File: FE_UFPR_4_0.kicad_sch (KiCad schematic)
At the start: 0 parts

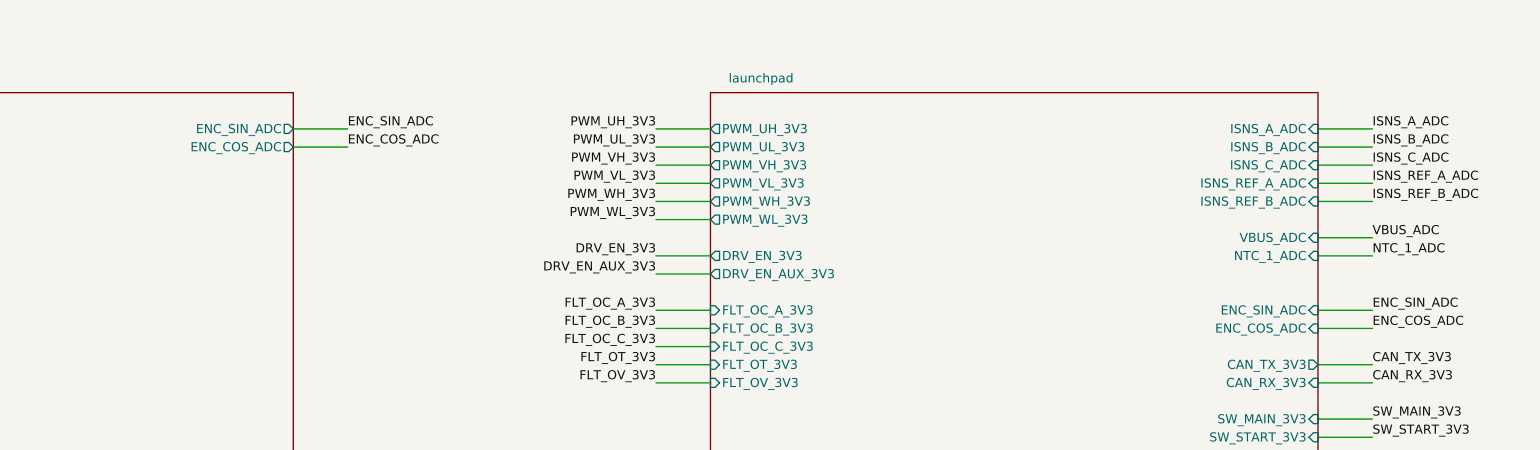
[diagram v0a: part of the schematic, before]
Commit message: S9.5: motor temperature channel (EMRAX KTY81-210) on J4 cavities 6/7
The board had no motor-temperature channel at all, and the EMRAX manual
makes one mandatory: the sensor "must be connected to the controller",
120 C on the copper windings voids the warranty, and on sensor
disconnection "the controller has to stop the motor". Captured now
because the board is placed but not yet routed.

Circuit: KTY81-210 as the divider's BOTTOM leg, excited from +3V3 through
R129 2.20k 0.1%. Open -> 3.30 V, short -> 0 V, both outside the valid
1.12-2.18 V band, so disconnect detection is free. +3V3 rather than +5V
so an open sensor cannot exceed the ADC's VDDA+0.3 absolute maximum.
6.25 codes/K at the 120 C limit. R131/R132 monitor the excitation rail on
ADCINA3 so firmware cancels it exactly - without that the LDO's +/-2 % is
+/-10 K, larger than the sensor's own +/-4.7 K.

J4 cavities 6/7 with 5/8 left empty as a guard column; ADC = ADCINB3 on
J20 pad 10. Zero new BOM lines - every part reuses an existing LCSC code.

GATED: legal only if EMRAX confirms the KTY is reinforced-insulated from
the windings. Basic insulation makes it a tractive-system conductor
(FSAE 2026 EV.1.6) and EV.6.5.3 forbids it sharing J4 with the encoder.

Also fixes a PRE-EXISTING defect: sync_schematic_to_board lists nets in
nets_added that it never assigns to pads. +5V_VEH and CAN_RS had ZERO pad
assignments on the board, including in the S9 commit - S10 would have
routed with the ECU supply feed and the CAN slope resistor unconnected.
All twelve pad assignments written directly and confirmed via KiCad's own
IPC-D-356 export.

Gates: netlist re-baselined 220/914 -> 219 nets / 933 nodes (delta fully
accounted); ERC --severity-all 0; DRC --severity-all 0 errors, parity 0.

Co-Authored-By: Claude Opus 5 (1M context) <noreply@anthropic.com>
Claude-Session: https://claude.ai/code/session_016KxKfBKo62GztNqtTupiHA
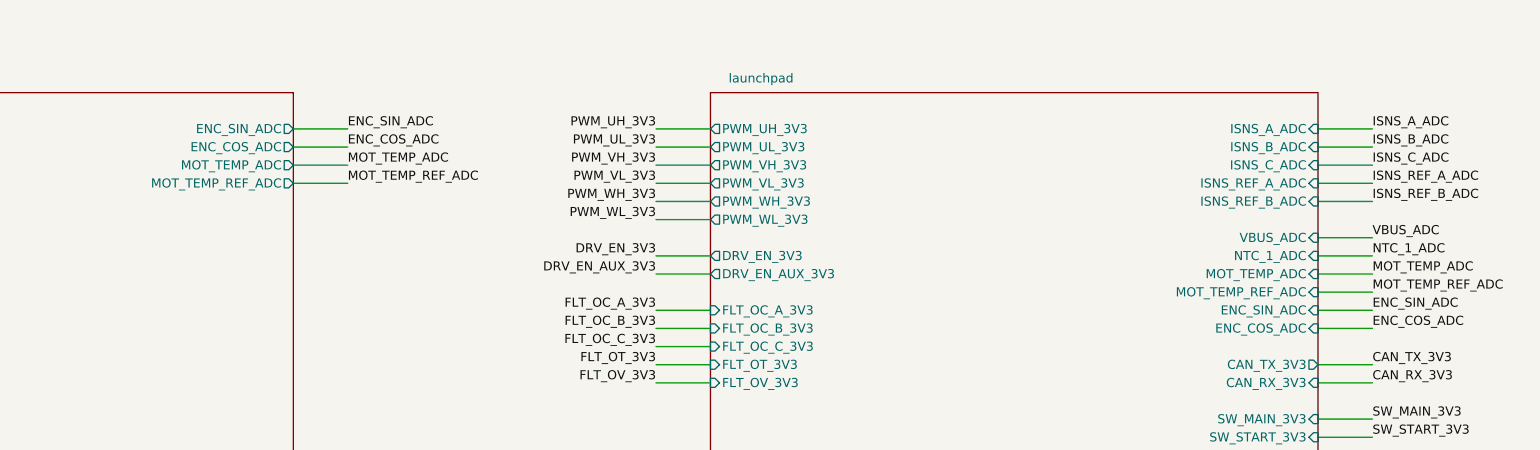
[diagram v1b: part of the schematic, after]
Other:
- sheet encoder ports: added MOT_TEMP_ADC, MOT_TEMP_REF_ADC; removed none
- sheet launchpad ports: added MOT_TEMP_ADC, MOT_TEMP_REF_ADC; removed none
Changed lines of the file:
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@@
+	(wire
+		(pts
+			(xy 214.63 125.73) (xy 222.25 125.73)
+		)
+		(stroke
+			(width 0)
+			(type default)
+		)
+	)
+	(label "MOT_TEMP_ADC"
+		(at 222.25 125.73 0)
+		(effects
+			(font
+				(size 1.27 1.27)
+			)
+			(justify left bottom)
+		)
+	)
+	(wire
+		(pts
+			(xy 214.63 128.27) (xy 222.25 128.27)
+		)
+		(stroke
+			(width 0)
+			(type default)
+		)
+	)
+	(label "MOT_TEMP_REF_ADC"
+		(at 222.25 128.27 0)
+		(effects
+			(font
+				(size 1.27 1.27)
+			)
+			(justify left bottom)
+		)
+	)
+	(wire
+		(pts
+			(xy 358.14 140.97) (xy 365.76 140.97)
+		)
+		(stroke
+			(width 0)
+			(type default)
+		)
+	)
+	(label "MOT_TEMP_ADC"
+		(at 365.76 140.97 0)
+		(effects
+			(font
+				(size 1.27 1.27)
+			)
+			(justify left bottom)
+		)
+	)
+	(wire
+		(pts
+			(xy 358.14 143.51) (xy 365.76 143.51)
+		)
+		(stroke
+			(width 0)
+			(type default)
+		)
+	)
+	(label "MOT_TEMP_REF_ADC"
+		(at 365.76 143.51 0)
+		(effects
+			(font
+				(size 1.27 1.27)
+			)
+			(justify left bottom)
+		)
+	)
 	(wire
 		(pts
@@
 			)
 		)
+		(pin "MOT_TEMP_ADC" input
+			(at 358.14 140.97 0)
+			(effects
+				(font
+					(size 1.27 1.27)
+				)
+				(justify right)
+			)
+		)
+		(pin "MOT_TEMP_REF_ADC" input
+			(at 358.14 143.51 0)
+			(effects
+				(font
+					(size 1.27 1.27)
+				)
+				(justify right)
+			)
+		)
 		(pin "CAN_TX_3V3" output
 			(at 358.14 153.67 0)
@@
 			(effects
 				(font
+					(size 1.27 1.27)
+				)
+				(justify right)
+			)
+		)
+		(pin "MOT_TEMP_ADC" output
+			(at 214.63 125.73 0)
+			(effects
+				(font
+					(size 1.27 1.27)
+				)
+				(justify right)
+			)
+		)
+		(pin "MOT_TEMP_REF_ADC" output
+			(at 214.63 128.27 0)
+			(effects
+				(font
